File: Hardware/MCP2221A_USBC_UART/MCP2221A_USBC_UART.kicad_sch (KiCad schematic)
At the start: 50 parts, among them J1 USB_C_Receptacle_USB2.0_16P, J2 Output Header, J3 3.3v IN/OUT, J4 USB 5v OUT, Q1 AO3400A, Q2 AO3400A, SW1 SW_PUSH, U1 USBLC6-4SC6, U2 MCP2221AxSL, U3 XC6220B331MR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

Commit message: Hardware updates and cleanup
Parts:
- removed C1: 22uF, Capacitor_SMD:C_0805_2012Metric_Pad1.18x1.45mm_HandSolder, symbol Device:C
- removed D1, D2: GREEN, LED_SMD:LED_0805_2012Metric_Pad1.15x1.40mm_HandSolder, symbol Device:LED
- removed D3: SMAJ5.0A, Diode_SMD:D_SMA, symbol Diode:SMAJ5.0A
- removed D7, D8: RED, LED_SMD:LED_0805_2012Metric_Pad1.15x1.40mm_HandSolder, symbol Device:LED
- removed J3: 3.3v IN/OUT, Connector_PinHeader_2.54mm:PinHeader_1x02_P2.54mm_Vertical, symbol Connector_Generic:Conn_01x02
- removed J4: USB 5v OUT, Connector_PinHeader_2.54mm:PinHeader_1x02_P2.54mm_Vertical, symbol Connector_Generic:Conn_01x02
- removed JP1: Power Select Jumper, Jumper:SolderJumper-2_P1.3mm_Open_RoundedPad1.0x1.5mm, symbol Jumper:SolderJumper_2_Open
- removed R18, R19, R7, R8: 1k, Resistor_SMD:R_0805_2012Metric_Pad1.20x1.40mm_HandSolder, symbol Device:R
- removed U1: USBLC6-4SC6, Package_TO_SOT_SMD:SOT-23-6, symbol Power_Protection:USBLC6-4SC6
- added J5: Conn_01x04, Connector_PinSocket_2.54mm:PinSocket_1x04_P2.54mm_Vertical, symbol Connector_Generic:Conn_01x04
- added JP1: SolderJumper_3_Open, Jumper:SolderJumper-3_P1.3mm_Open_RoundedPad1.0x1.5mm, symbol Jumper:SolderJumper_3_Open
- added U1: USBLC6-2SC6, Package_TO_SOT_SMD:SOT-23-6, symbol Power_Protection:USBLC6-2SC6
- SW1: footprint General:SW_SPST -> Button_Switch_SMD:SW_SPST_PTS645Sx43SMTR92
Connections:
- net +3.3V: now also JP1.1 (A)
- net +3.3VA: now also JP1.2 (C)
- net +5V: now also J5.4 (Pin_4), U1.5 (VBUS)
- net D+: now also U1.4 (I/O2); no longer J1.A6 (D+), J1.B6 (D+)
- net D-: now also U1.6 (I/O1); no longer J1.A7 (D-), J1.B7 (D-)
- net GND: now also R4.1, J5.2 (Pin_2), J5.3 (Pin_3), U1.2 (GND); no longer R4.2
- net IOA: now also J2.2 (Pin_2); no longer J2.1 (Pin_1)
- net IOB: now also J2.1 (Pin_1); no longer J2.2 (Pin_2)
- net RXB: now also J2.3 (Pin_3); no longer J2.6 (Pin_6)
- net SCLB: now also J2.6 (Pin_6); no longer J2.4 (Pin_4)
- net SDAB: now also J2.5 (Pin_5); no longer J2.3 (Pin_3)
- net TXB: now also J2.4 (Pin_4); no longer J2.5 (Pin_5)
- net at Q2.1 (G), R2.2: now also R4.2; no longer R4.1
- new net: J5.1 (Pin_1), JP1.3 (B)
- new net: J1.A7 (D-), J1.B7 (D-), U1.1 (I/O1)
- new net: J1.A6 (D+), J1.B6 (D+), U1.3 (I/O2)
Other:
- note added: "Jump JP1 to power the line buffers from either the on board LDO or external 3.3v"
- note removed: "Bridge JP1 to power buffers from on-board LDO Unbridge when external power is desired Bridged will make J3-3 a 3.3v output Unbridged required 3.3v to be applied to J3-3"
- moved on the sheet: R4

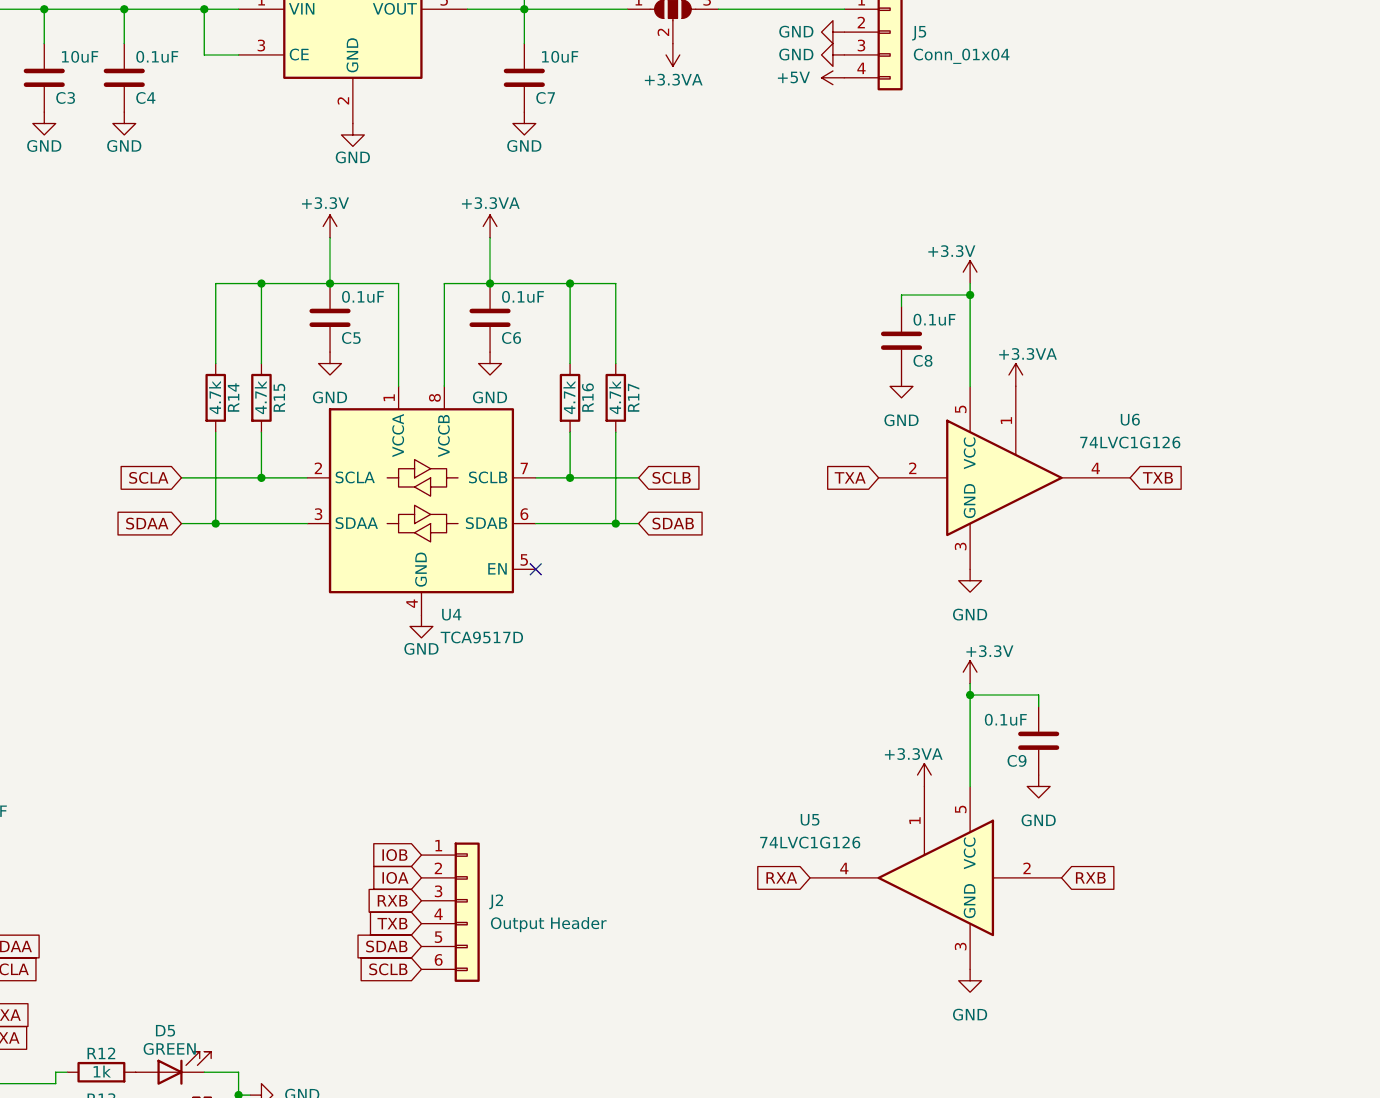
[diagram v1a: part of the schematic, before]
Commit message: Hardware updates. Add Lr04 lora module datasheets
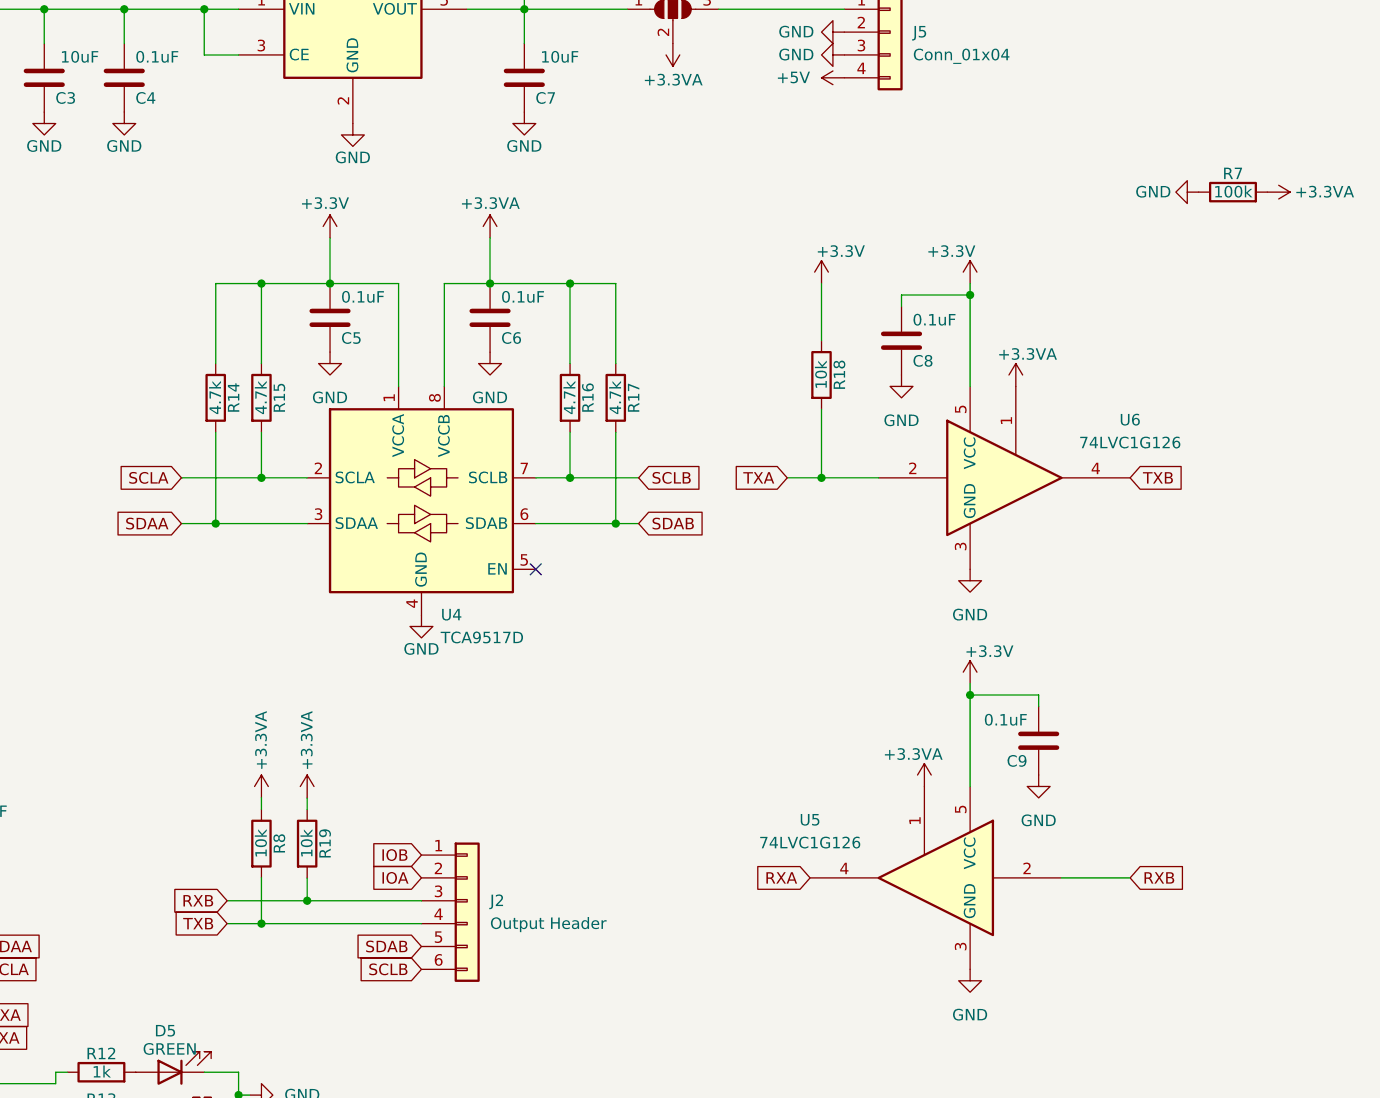
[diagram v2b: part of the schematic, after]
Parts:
- added R18, R19, R8: 10k, Resistor_SMD:R_0805_2012Metric_Pad1.20x1.40mm_HandSolder, symbol Device:R
- added R7: 100k, Resistor_SMD:R_0805_2012Metric_Pad1.20x1.40mm_HandSolder, symbol Device:R
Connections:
- net +3.3V: now also R18.1
- net +3.3VA: now also R19.1, R7.2, R8.1
- net GND: now also R7.1
- net RXB: now also R19.2
- net TXA: now also R18.2
- net TXB: now also R8.2
